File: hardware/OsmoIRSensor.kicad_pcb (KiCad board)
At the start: 2 copper layers, 9.5 x 22 mm, 11 parts, among them J2 CONN_02X03_PCB_DIRECT, U1 ATTINY45-S, U2 TSOP75436WTR, X1 20MHz

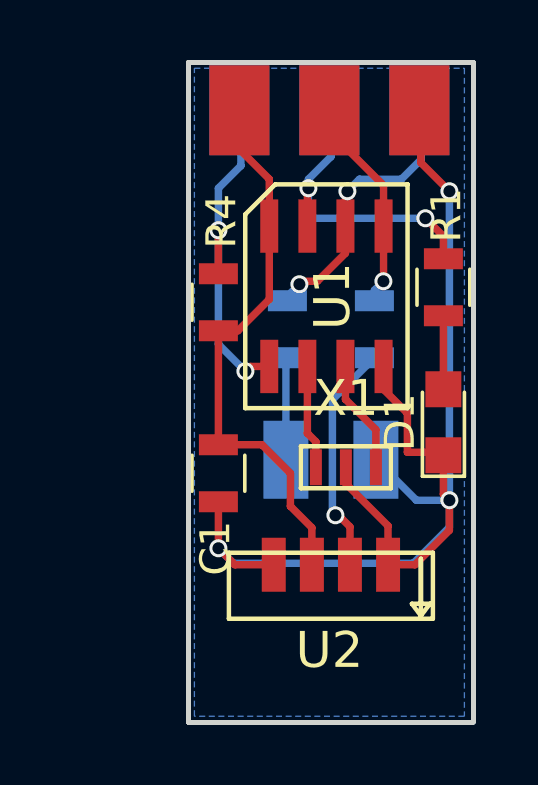
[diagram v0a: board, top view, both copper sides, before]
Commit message: - Corrected IC Pads Size - Gerber Files added for 10x9,1cm panelized pcb - 3D Printer Files for optical Barrier added - Pin Desc. for DEV Cabel
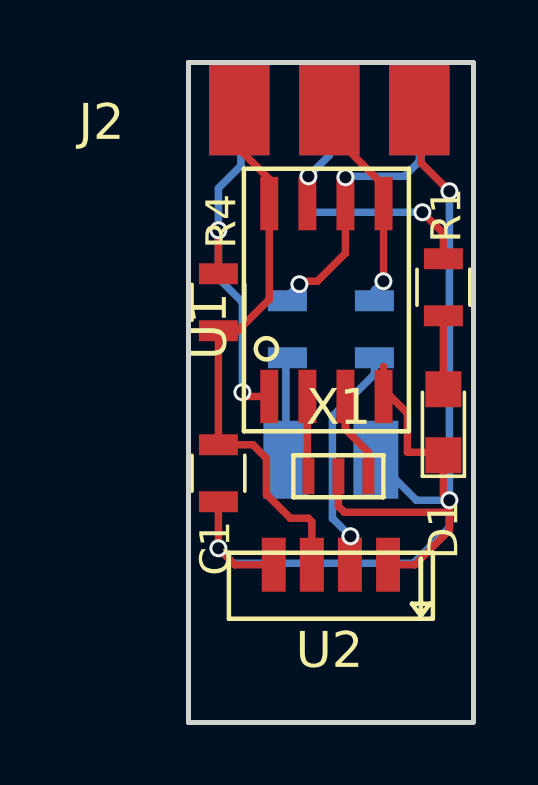
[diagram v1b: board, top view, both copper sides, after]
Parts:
- moved X1 0.39 mm to (142.2, 99.8)
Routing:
- net GND: track 42.8 -> 43.9 mm
- net Net-(J2-Pad5): track 11.1 -> 10.1 mm
- net Net-(U1-Pad2): track 3.48 -> 2.67 mm
- net Net-(J2-Pad6): track 11.8 -> 12.5 mm
- net Net-(J2-Pad4): track 11.3 -> 11.8 mm
- removed copper zone on B.Cu, net GND
